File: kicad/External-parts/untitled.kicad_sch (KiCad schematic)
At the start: 1 part, among them J1 Joystick

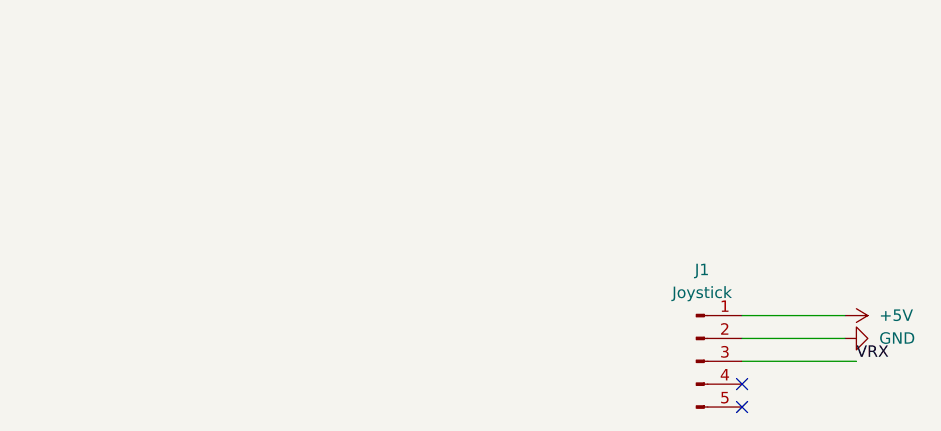
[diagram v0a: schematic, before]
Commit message: add ultrasonic, speaker, nhd
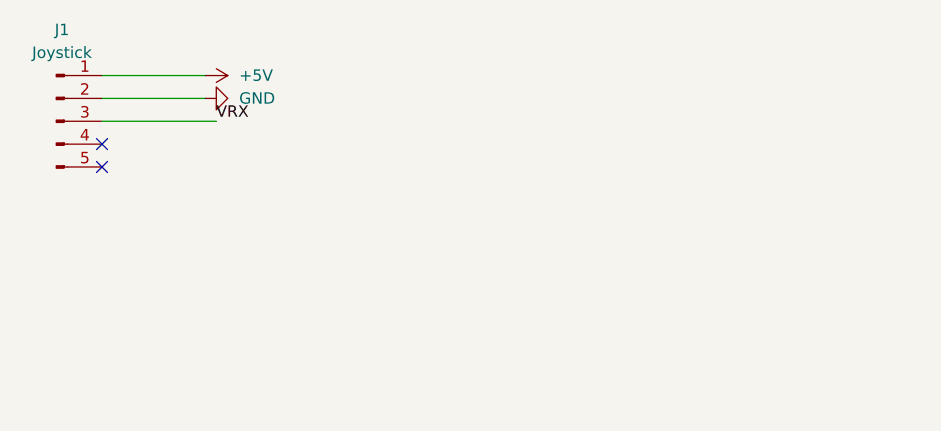
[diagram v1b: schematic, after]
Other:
- company: (none) -> ECE 47700 Team 01
- title: (none) -> Offboard 8-Ohm Speaker
- moved on the sheet: J1
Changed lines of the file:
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@@
 	(generator "eeschema")
 	(generator_version "8.0")
-	(paper "A4")
+	(paper "User" 177.8 127)
+	(title_block
+		(title "Offboard 8-Ohm Speaker")
+		(company "ECE 47700 Team 01")
+	)
 	(no_connect
-		(at 142.24 85.09)
+		(at 71.12 58.42)
 	)
 	(no_connect
-		(at 142.24 82.55)
+		(at 71.12 55.88)
 	)
 	(wire
 		(pts
-			(xy 142.24 80.01) (xy 154.94 80.01)
+			(xy 71.12 53.34) (xy 83.82 53.34)
 		)
 		(stroke
@@
 	(wire
 		(pts
-			(xy 142.24 74.93) (xy 153.67 74.93)
+			(xy 71.12 48.26) (xy 82.55 48.26)
 		)
 		(stroke
@@
 	(wire
 		(pts
-			(xy 142.24 77.47) (xy 153.67 77.47)
+			(xy 71.12 50.8) (xy 82.55 50.8)
 		)
 		(stroke
@@
 	)
 	(label "VRX"
-		(at 154.94 80.01 0)
+		(at 83.82 53.34 0)
 		(effects
 			(font
@@
 	(symbol
 		(lib_id "power:+5V")
-		(at 153.67 74.93 270)
+		(at 82.55 48.26 270)
 		(unit 1)
 		(exclude_from_sim no)
@@
 		(fields_autoplaced yes)
 		(property "Reference" "#PWR05"
-			(at 149.86 74.93 0)
+			(at 78.74 48.26 0)
 			(effects
 				(font
@@
 		)
 		(property "Value" "+5V"
-			(at 157.48 74.9299 90)
+			(at 86.36 48.2599 90)
 			(effects
 				(font
@@
 		)
 		(property "Footprint" ""
-			(at 153.67 74.93 0)
+			(at 82.55 48.26 0)
 			(effects
 				(font
@@
 		)
 		(property "Datasheet" ""
-			(at 153.67 74.93 0)
+			(at 82.55 48.26 0)
 			(effects
 				(font
@@
 		)
 		(property "Description" "Power symbol creates a global label with name \"+5V\""
-			(at 153.67 74.93 0)
+			(at 82.55 48.26 0)
 			(effects
 				(font
@@
 	(symbol
 		(lib_id "power:GND")
-		(at 153.67 77.47 90)
+		(at 82.55 50.8 90)
 		(unit 1)
 		(exclude_from_sim no)
@@
 		(dnp no)
 		(property "Reference" "#PWR06"
-			(at 160.02 77.47 0)
+			(at 88.9 50.8 0)
 			(effects
 				(font
@@
 		)
 		(property "Value" "GND"
-			(at 157.48 77.4699 90)
+			(at 86.36 50.7999 90)
 			(effects
 				(font
@@
 		)
 		(property "Footprint" ""
-			(at 153.67 77.47 0)
+			(at 82.55 50.8 0)
 			(effects
 				(font
@@
 		)
 		(property "Datasheet" ""
-			(at 153.67 77.47 0)
+			(at 82.55 50.8 0)
 			(effects
 				(font
@@
 		)
 		(property "Description" "Power symbol creates a global label with name \"GND\" , ground"
-			(at 153.67 77.47 0)
+			(at 82.55 50.8 0)
 			(effects
 				(font
@@
 	(symbol
 		(lib_id "Connector:Conn_01x05_Pin")
-		(at 137.16 80.01 0)
+		(at 66.04 53.34 0)
 		(unit 1)
 		(exclude_from_sim no)
@@
 		(fields_autoplaced yes)
 		(property "Reference" "J1"
-			(at 137.795 69.85 0)
+			(at 66.675 43.18 0)
 			(effects
 				(font
@@
 		)
 		(property "Value" "Joystick"
-			(at 137.795 72.39 0)
+			(at 66.675 45.72 0)
 			(effects
 				(font
@@
 		)
 		(property "Footprint" ""
-			(at 137.16 80.01 0)
+			(at 66.04 53.34 0)
 			(effects
 				(font
@@
 		)
 		(property "Datasheet" "~"
-			(at 137.16 80.01 0)
+			(at 66.04 53.34 0)
 			(effects
 				(font
@@
 		)
 		(property "Description" "Generic connector, single row, 01x05, script generated"
-			(at 137.16 80.01 0)
-			(effects
-				(font
+			(at 66.04 53.34 0)
+			(effects
+				(font
